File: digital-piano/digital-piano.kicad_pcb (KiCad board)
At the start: 2 copper layers, 116.8 x 71.1 mm, 20 parts, among them J1 Conn_01x22, J10 Conn_01x01, J11 Conn_01x01, J12 Conn_01x01, J13 Conn_01x01, J14 Conn_01x01, J15 Conn_01x01, J16 Conn_01x01, J2 Conn_01x22, J3 Conn_01x01, J4 Conn_01x01, J5 Conn_01x01, J6 Conn_01x01, J7 Conn_01x01, J8 Conn_01x01, J9 Conn_01x01

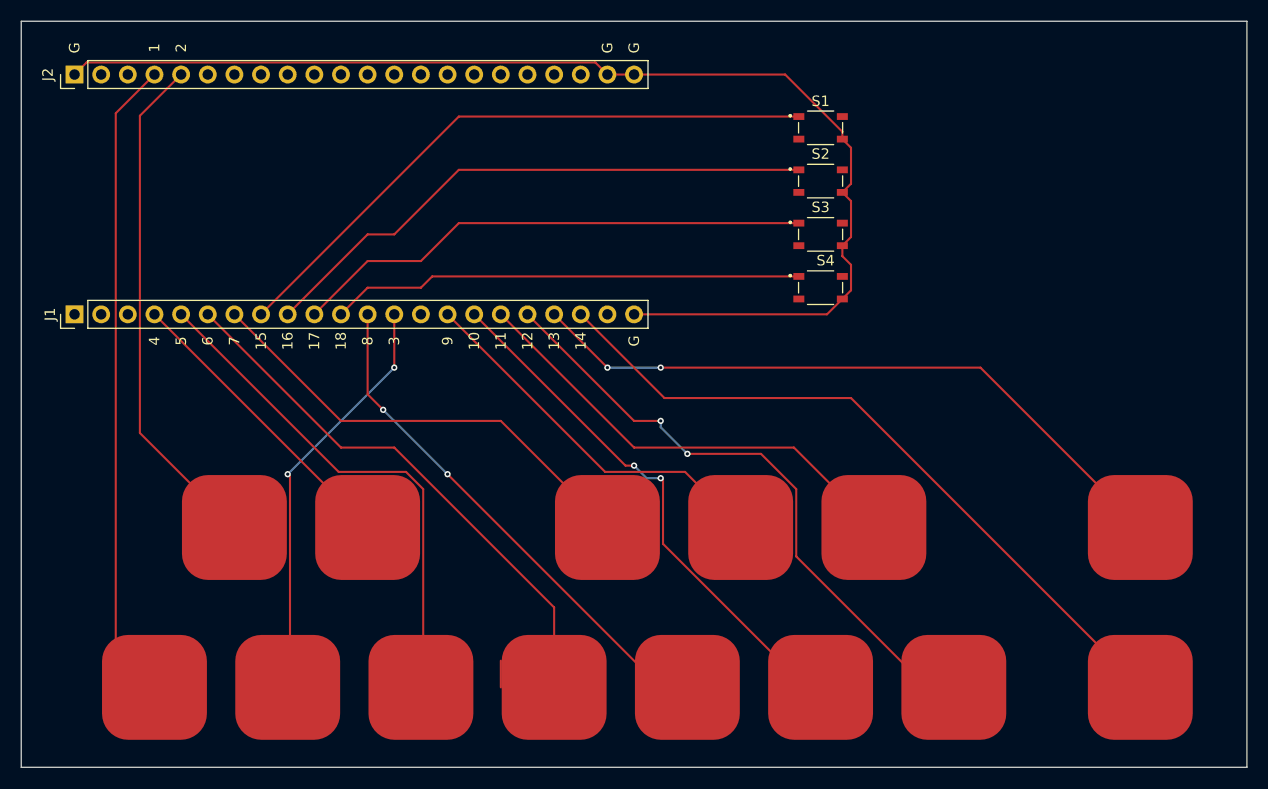
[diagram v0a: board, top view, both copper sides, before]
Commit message: Change PCB size of piano because of fablication price
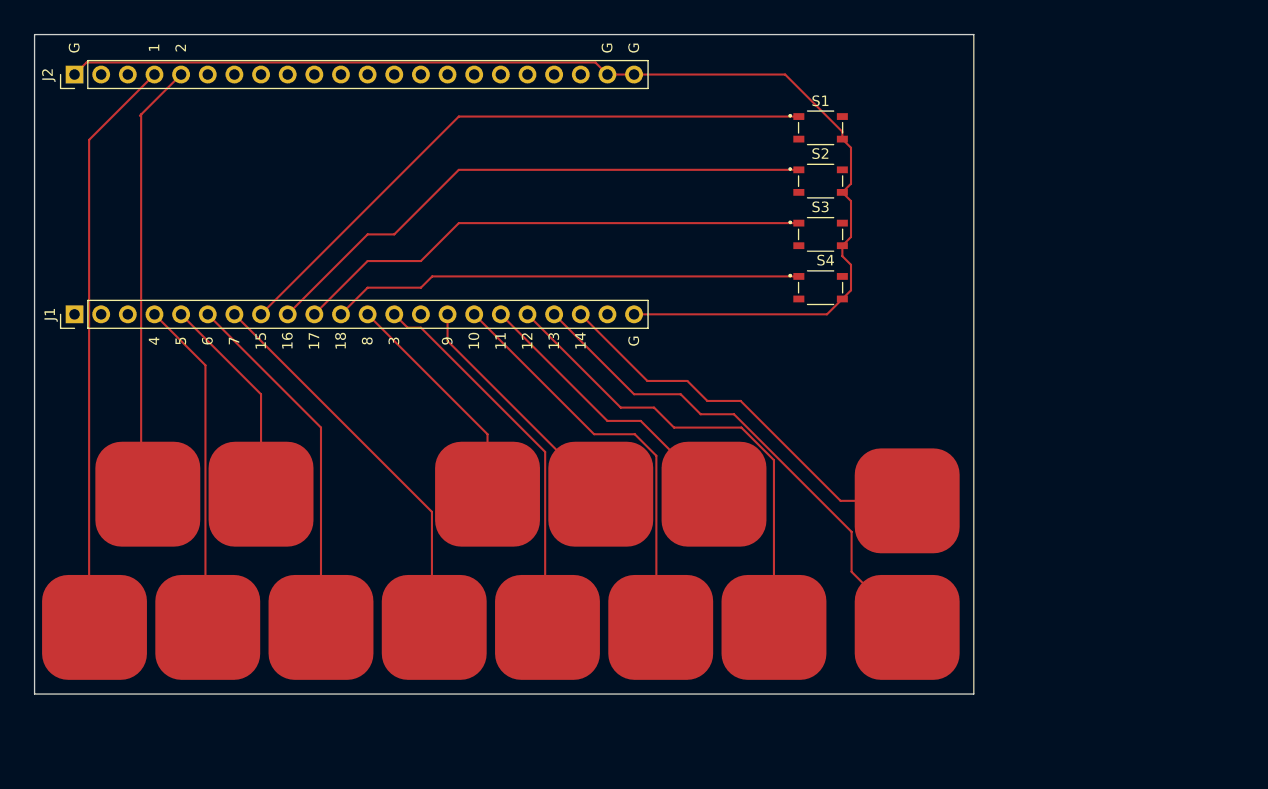
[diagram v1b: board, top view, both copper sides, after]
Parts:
- moved J15 28.5 mm to (102.2, 76.2)
- moved J10 26.5 mm to (62.2, 75.6)
- moved J5 25.4 mm to (67.9, 88.3)
- moved J16 24.2 mm to (102.2, 88.3)
- moved J7 23.9 mm to (40.6, 75.6)
- moved J8 22.9 mm to (46.4, 88.3)
- moved J9 19.1 mm to (57.1, 88.3)
- moved J14 18.1 mm to (89.5, 88.3)
- moved J6 18.0 mm to (35.6, 88.3)
- moved J12 16.3 mm to (78.7, 88.3)
- moved J13 15.6 mm to (83.8, 75.6)
- moved J11 13.7 mm to (73.0, 75.6)
- moved J4 8.84 mm to (29.8, 75.6)
- moved J3 8.08 mm to (24.8, 88.3)
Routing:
- net TOUCH5: track 50.6 -> 20.3 mm
- net TOUCH14: track 68.1 -> 38.5 mm
- net TOUCH8: track 49.7 -> 21.9 mm, vias 2 -> 0
- net TOUCH6: track 54.8 -> 34.3 mm
- net TOUCH11: track 44.0 -> 27.4 mm
- net TOUCH13: track 64.3 -> 48.2 mm, vias 2 -> 0
- net TOUCH12: track 59.5 -> 45.2 mm, vias 2 -> 0
- net TOUCH9: track 36.4 -> 23.2 mm
- net TOUCH10: track 51.6 -> 39.5 mm, vias 2 -> 0
- net TOUCH2: track 48.5 -> 42.0 mm
- net TOUCH7: track 44.0 -> 37.7 mm
- net TOUCH1: track 61.5 -> 55.5 mm
- net TOUCH3: track 40.3 -> 36.6 mm, vias 2 -> 0
- net TOUCH4: track 28.7 -> 31.9 mm
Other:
- board size 116.8 x 71.1 mm -> 89.5 x 62.9 mm
